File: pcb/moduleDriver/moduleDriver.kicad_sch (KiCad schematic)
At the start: 39 parts, among them J1 MOTOR, J10 Sensor, J11 Power, J12 Power, J13 Power, J14 LOOPBACK, J2 MOTOR, J3 MOTOR, J4 MOTOR, J5 IDC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

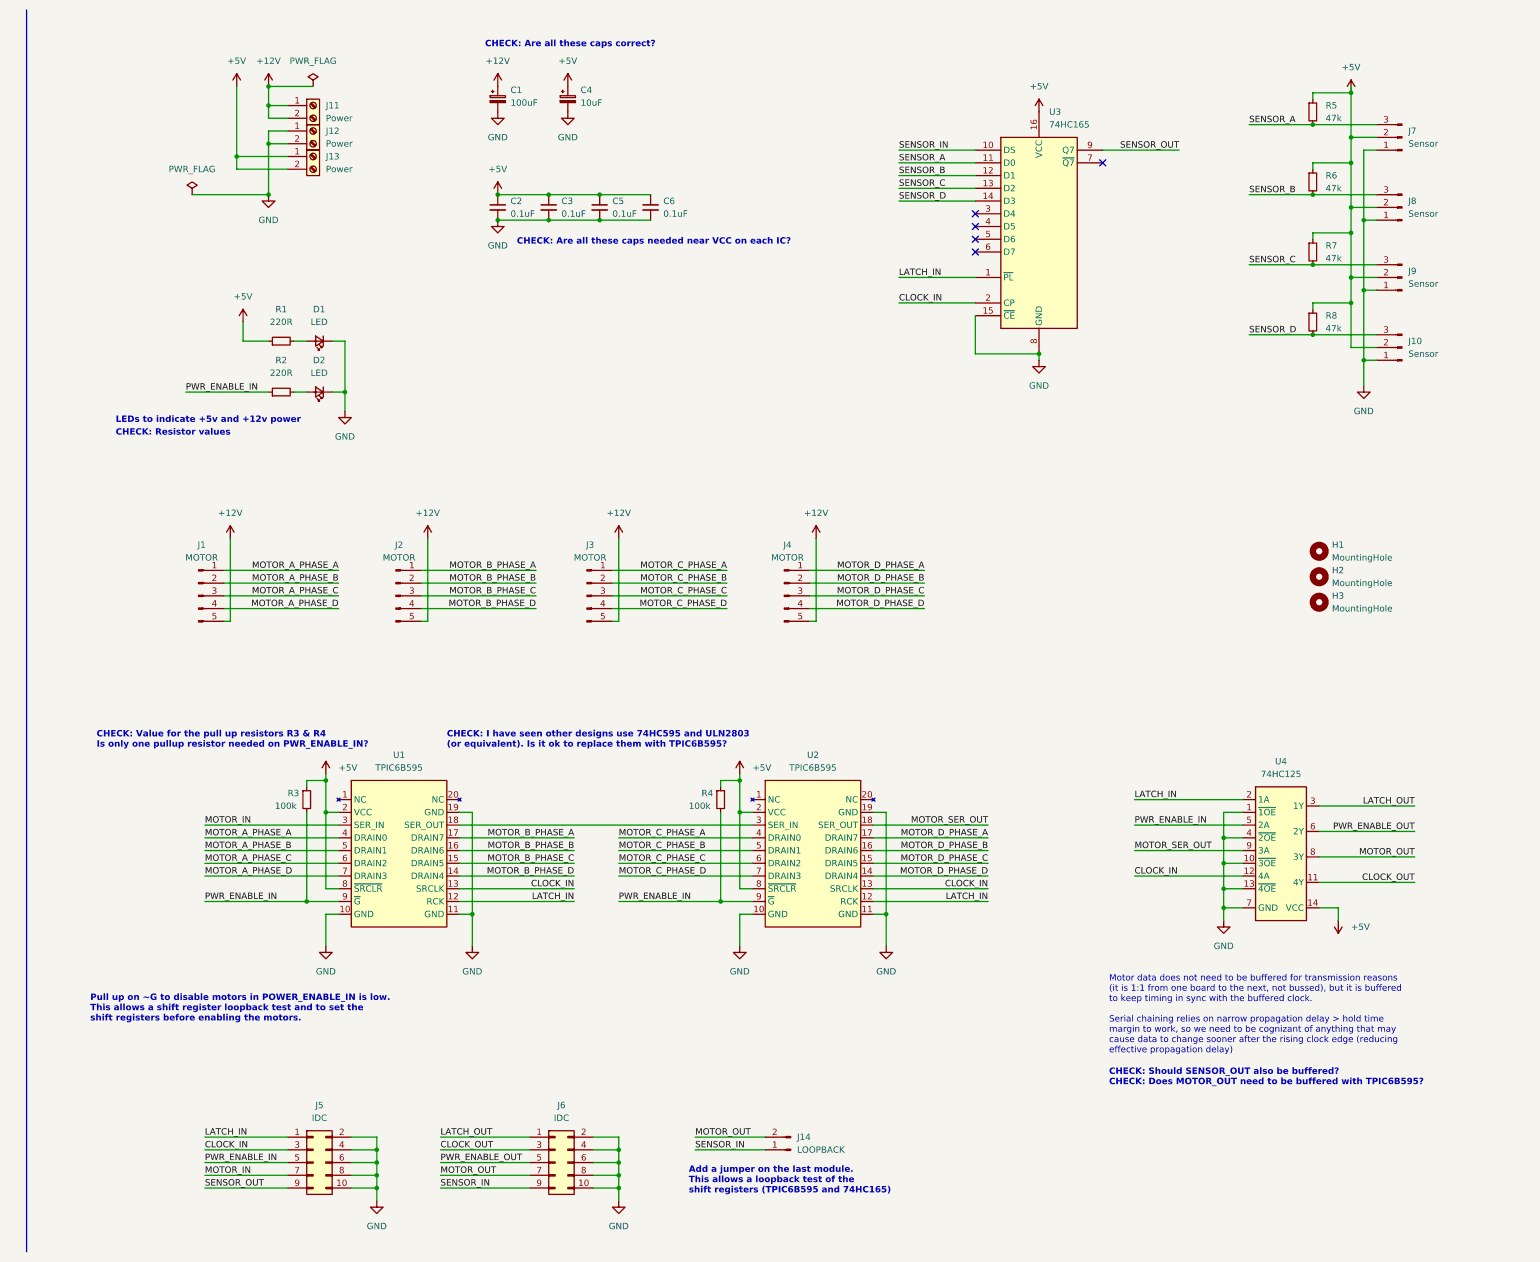
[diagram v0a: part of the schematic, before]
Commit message: Simple PCB fixes
- Change C2, C3, C5, C6 all to 1uF
- Delete R4
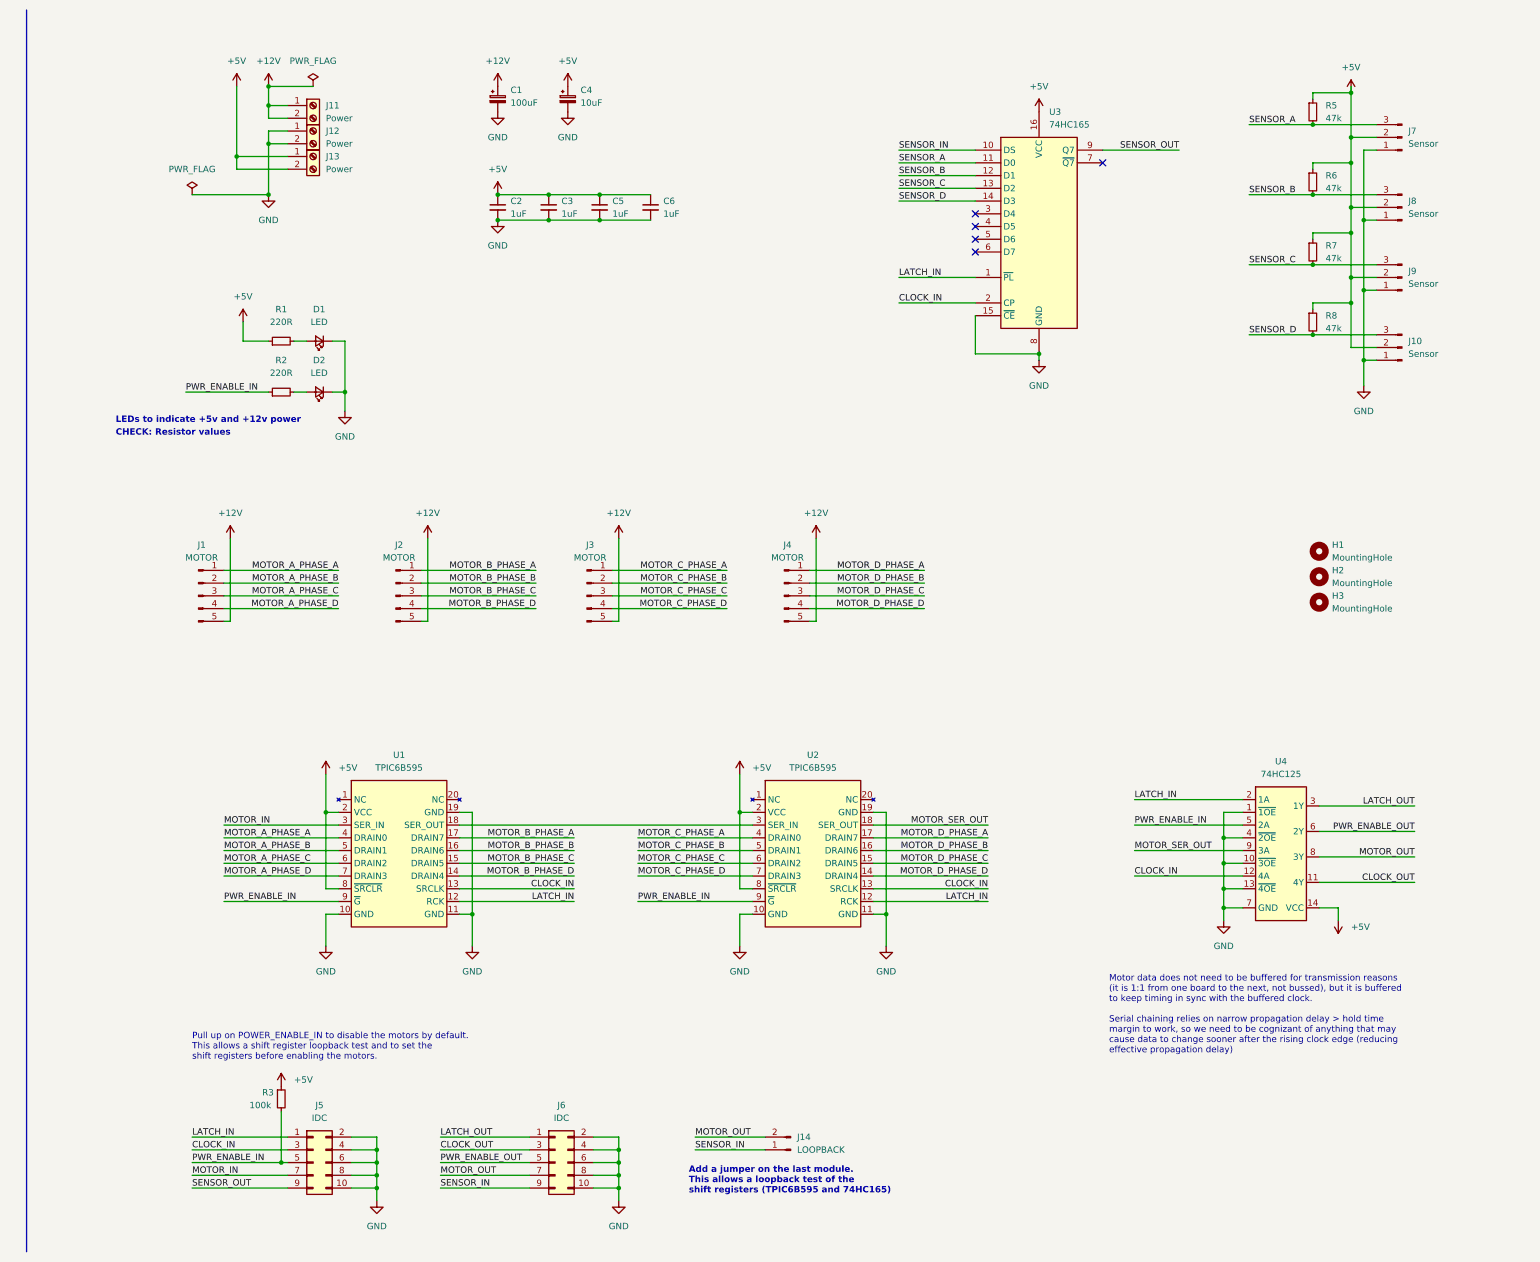
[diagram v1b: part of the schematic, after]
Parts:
- removed R4: 100k, Resistor_SMD:R_0603_1608Metric, symbol Device:R_Small
- C2, C3, C5, C6: value 0.1uF -> 1uF
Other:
- note added: "Pull up on POWER_ENABLE_IN to disable the motors by default. This allows a shift register loopback test and to set the shift registers before enabling the motors."
- note removed: "CHECK: Are all these caps correct?"
- note removed: "CHECK: Are all these caps needed near VCC on each IC?"
- note removed: "CHECK: I have seen other designs use 74HC595 and ULN2803 (or equivalent). Is it ok to replace them with TPIC6B595?"
- note removed: "CHECK: Should SENSOR_OUT also be buffered? CHECK: Does MOTOR_OUT need to be buffered with TPIC6B595?"
- note removed: "CHECK: Value for the pull up resistors R3 & R4 Is only one pullup resistor needed on PWR_ENABLE_IN?"
- note removed: "Pull up on ~G to disable motors in POWER_ENABLE_IN is low. This allows a shift register loopback test and to set the shift registers before enabling the motors."
- moved on the sheet: R3

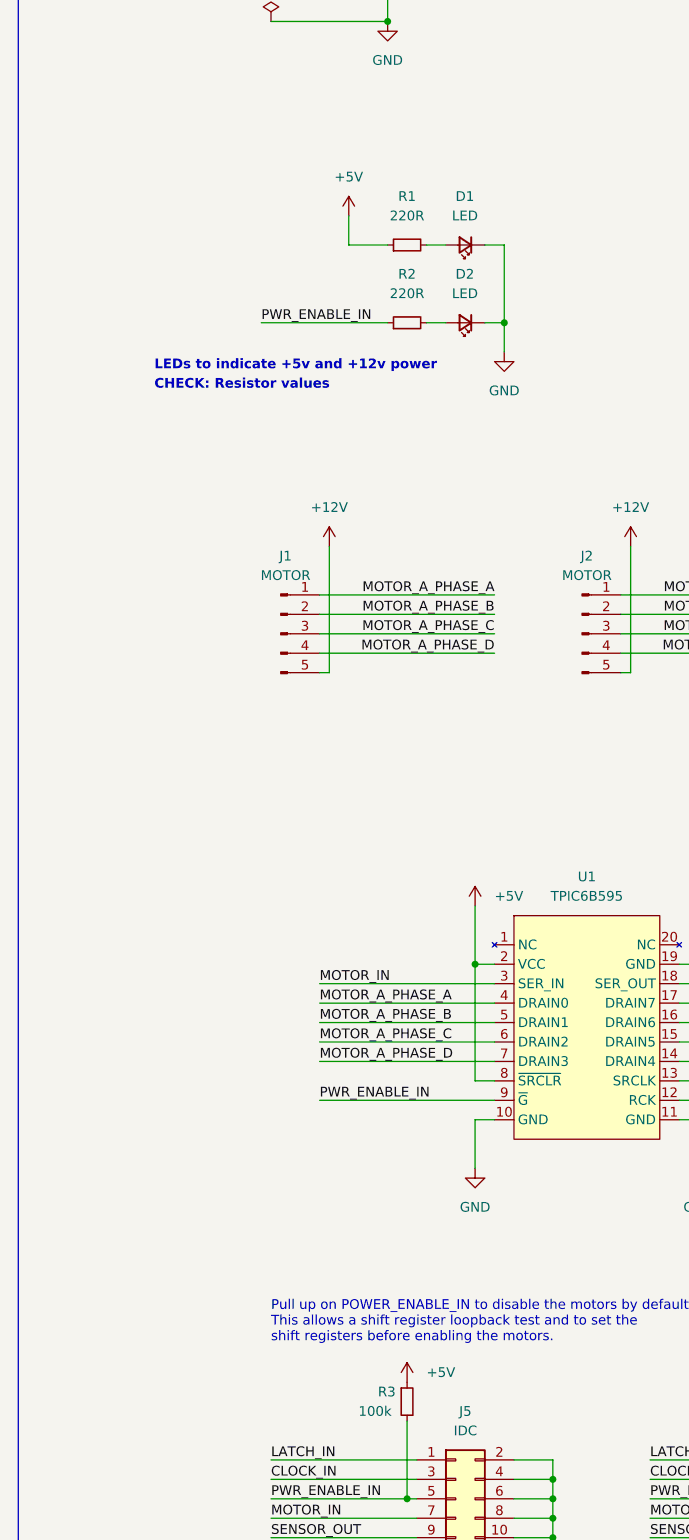
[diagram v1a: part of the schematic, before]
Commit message: Added 12v led
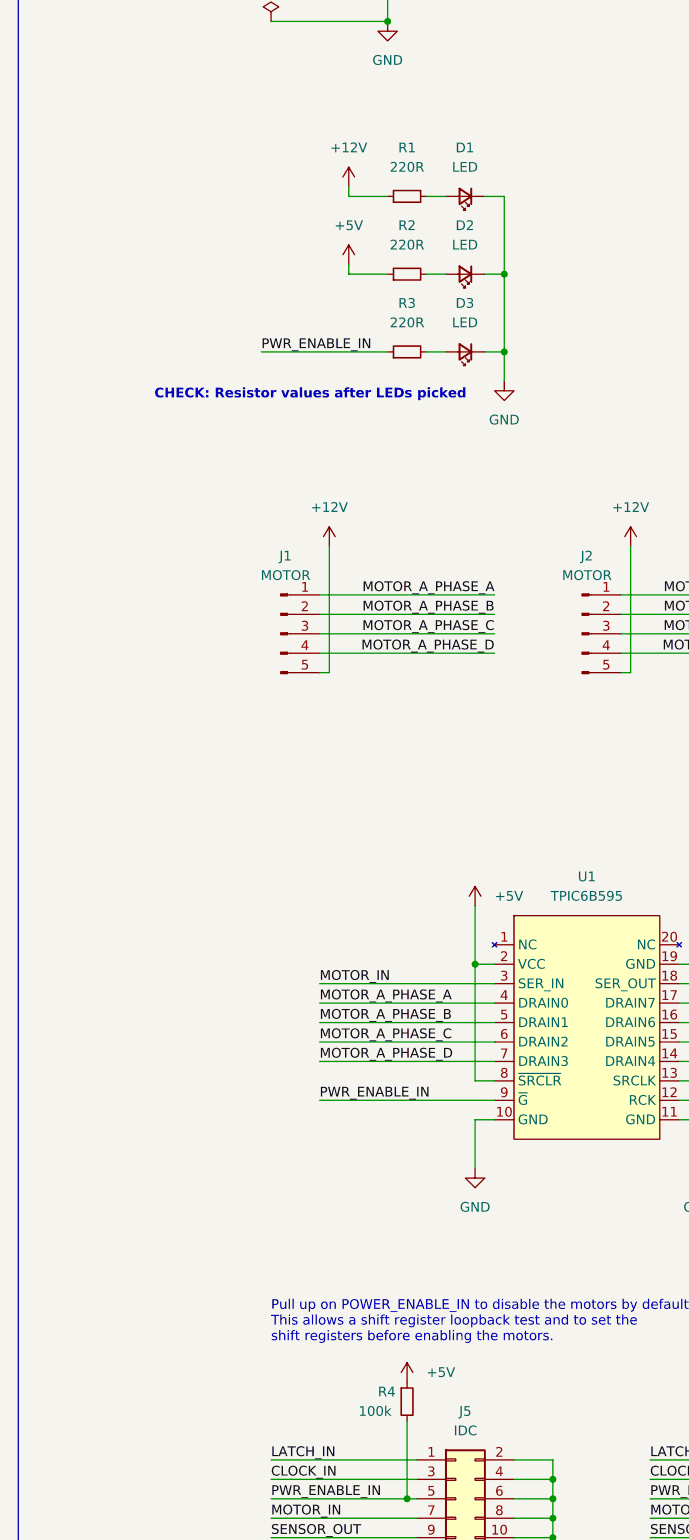
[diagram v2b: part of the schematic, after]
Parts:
- added D1: LED, LED_SMD:LED_0603_1608Metric, symbol Device:LED_Small
- added R1: 220R, Resistor_SMD:R_0603_1608Metric, symbol Device:R_Small
- renumbered D1 to D2, D2 to D3, R1 to R2, R2 to R3, R3 to R4
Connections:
- net +12V: now also R1.1
- net GND: now also D1.1 (K)
- new net: D1.2 (A), R1.2
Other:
- note added: "CHECK: Resistor values after LEDs picked"
- note removed: "CHECK: Resistor values"
- note removed: "LEDs to indicate +5v and +12v power"
- moved on the sheet: D2, D3, R2, R3

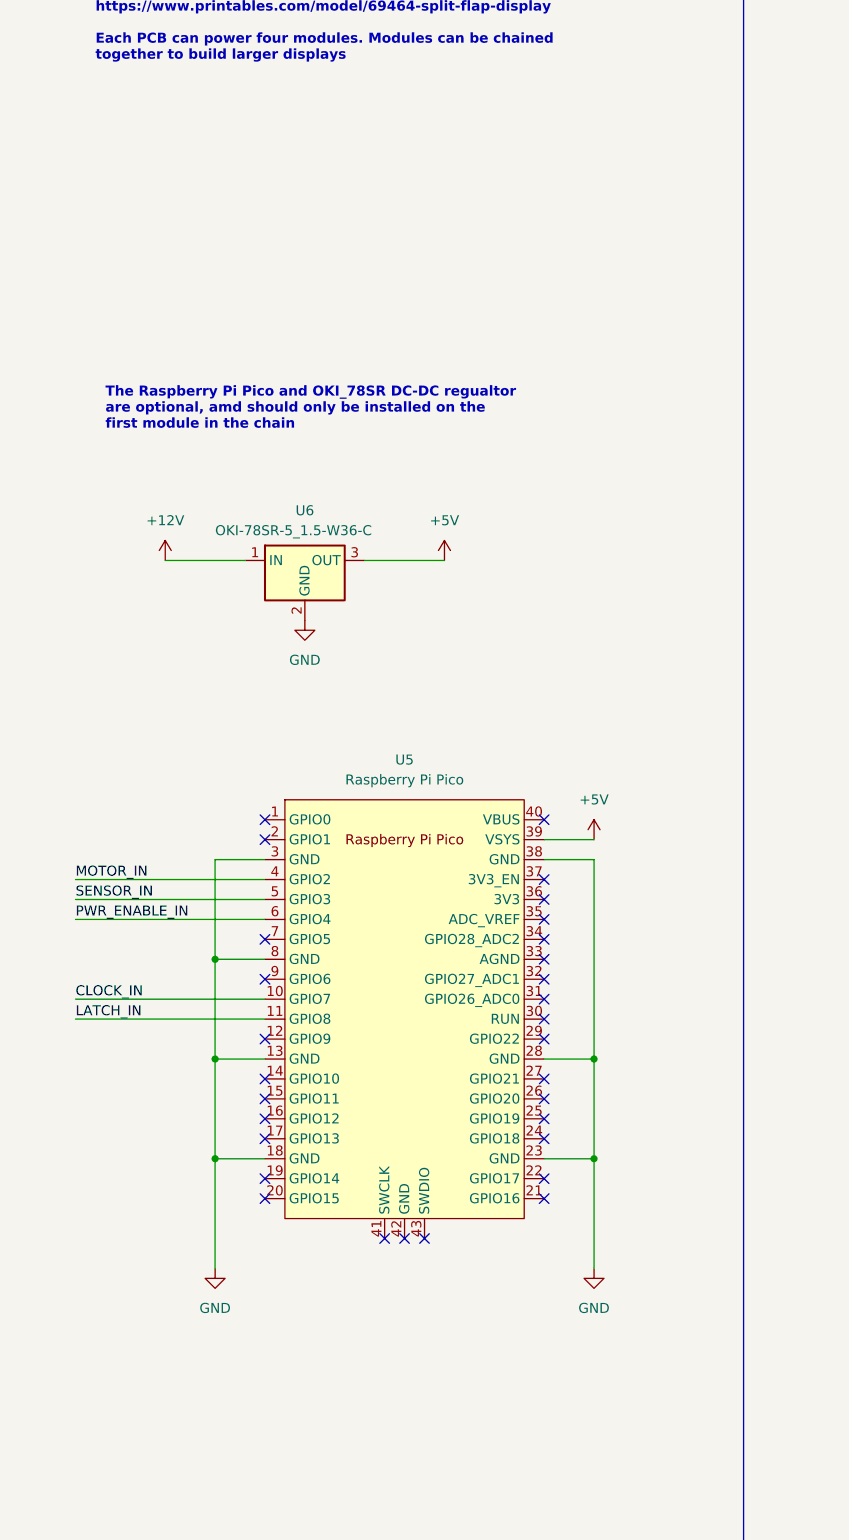
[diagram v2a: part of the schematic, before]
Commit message: Added level translation IC and pull up on PWR_ENABLE_IN_3V3
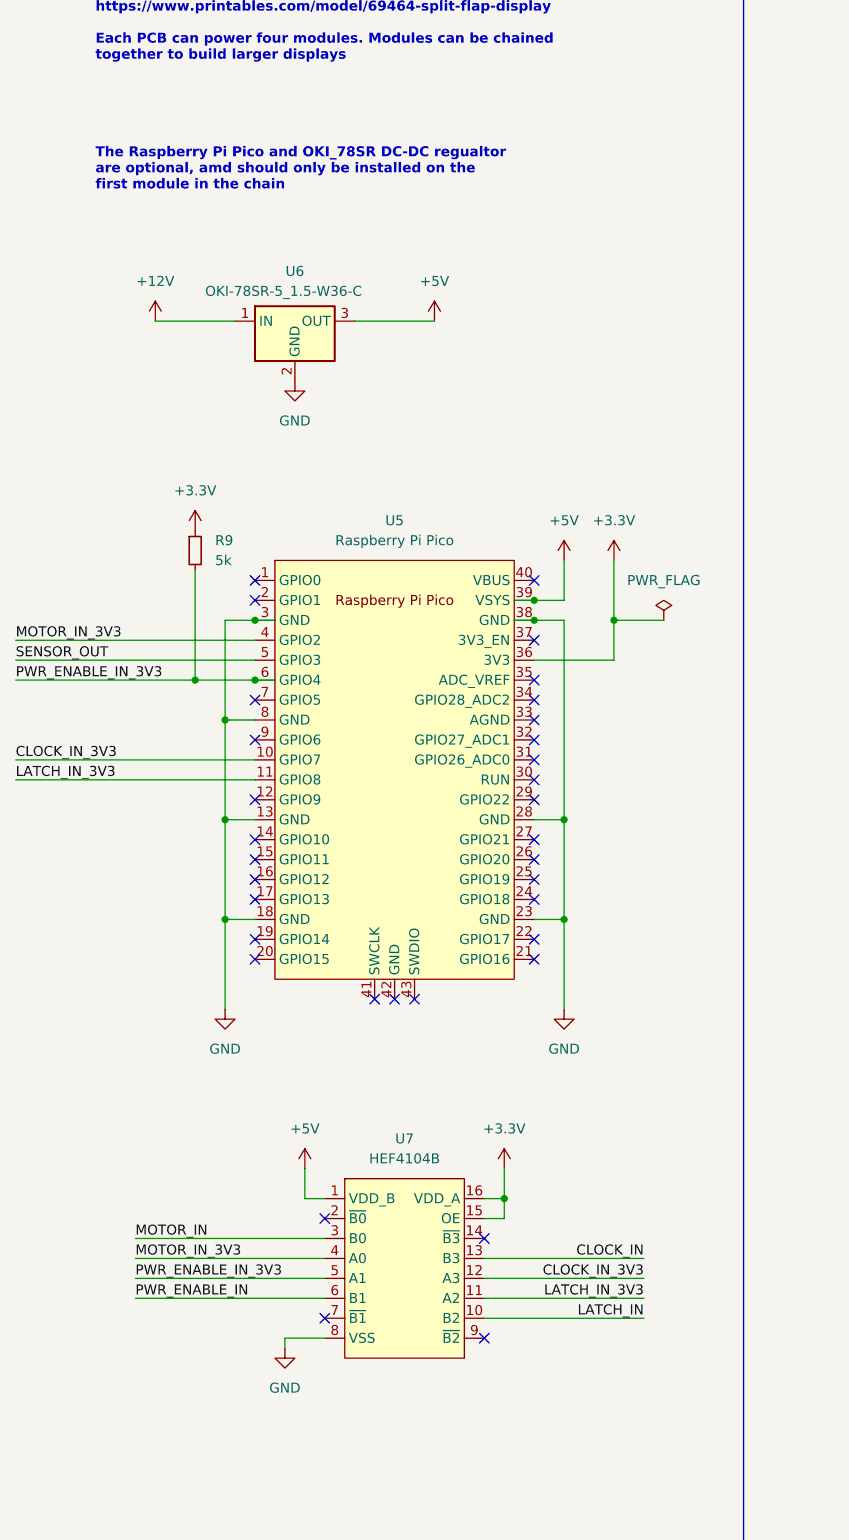
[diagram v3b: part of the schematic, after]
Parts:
- added R9: 5k, Resistor_SMD:R_0603_1608Metric, symbol Device:R_Small
- added U7: HEF4104B, symbol New_Library:HEF4104B
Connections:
- net +5V: now also U7.1 (VDD_B)
- net CLOCK_IN: now also U7.13 (B3); no longer U5.10 (GPIO7)
- net GND: now also U7.8 (VSS)
- net LATCH_IN: now also U7.10 (B2); no longer U5.11 (GPIO8)
- net MOTOR_IN: now also U7.3 (B0); no longer U5.4 (GPIO2)
- net PWR_ENABLE_IN: now also U7.6 (B1); no longer U5.6 (GPIO4)
- net SENSOR_IN: no longer U5.5 (GPIO3)
- net SENSOR_OUT: now also U5.5 (GPIO3)
- net +3.3V: now reaches U5.36 (3V3)
- net +3.3V: now also R9.1, U7.15 (OE), U7.16 (VDD_A)
- new net CLOCK_IN_3V3: U5.10 (GPIO7), U7.12 (A3)
- new net LATCH_IN_3V3: U5.11 (GPIO8), U7.11 (A2)
- new net MOTOR_IN_3V3: U5.4 (GPIO2), U7.4 (A0)
- new net PWR_ENABLE_IN_3V3: R9.2, U5.6 (GPIO4), U7.5 (A1)
- no-connect marks 35 -> 38
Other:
- moved on the sheet: U5, U6
